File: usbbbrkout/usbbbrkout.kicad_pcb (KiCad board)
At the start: 4 copper layers, 27.7 x 20.3 mm, 12 parts, among them P101 CONN_01X01, P102 CONN_01X01, P103 CONN_01X01, P104 CONN_01X01, P105 USB_B

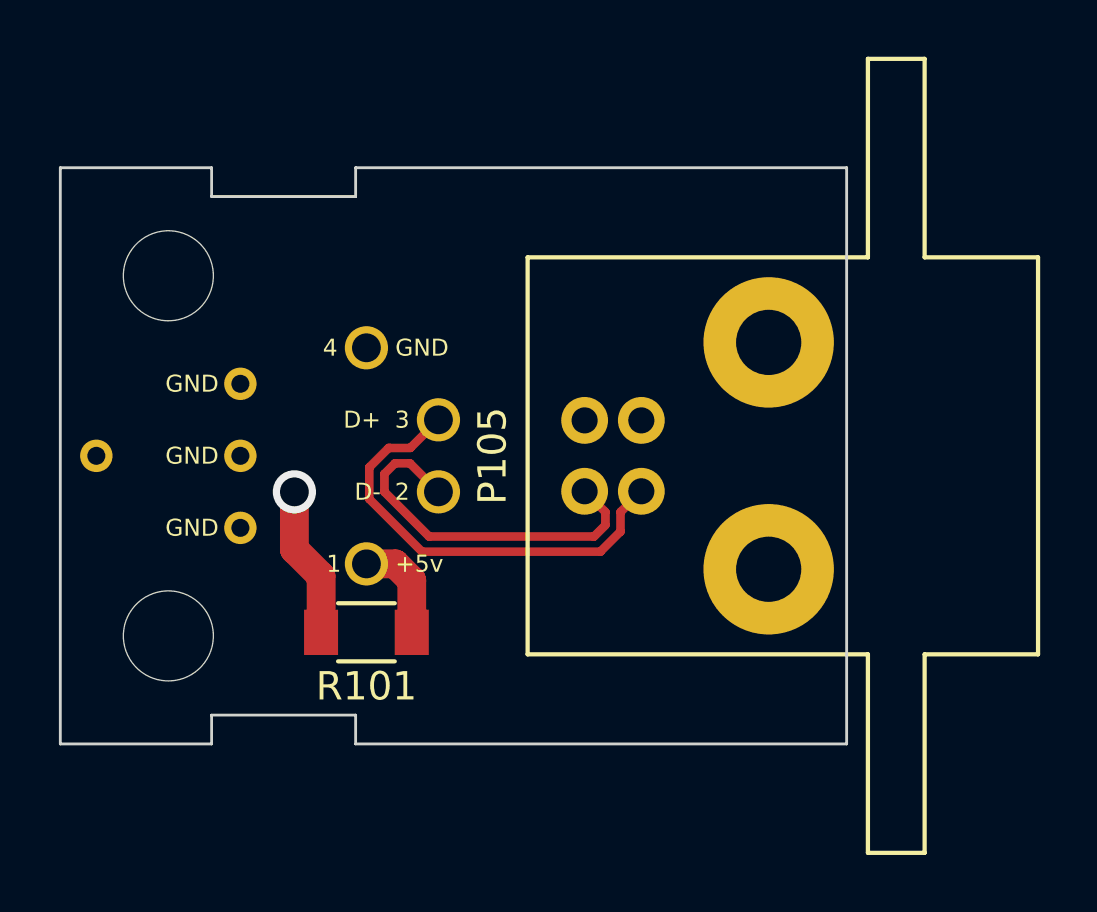
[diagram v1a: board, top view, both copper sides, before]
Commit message: Adjust clearances of ground and vcc pours.
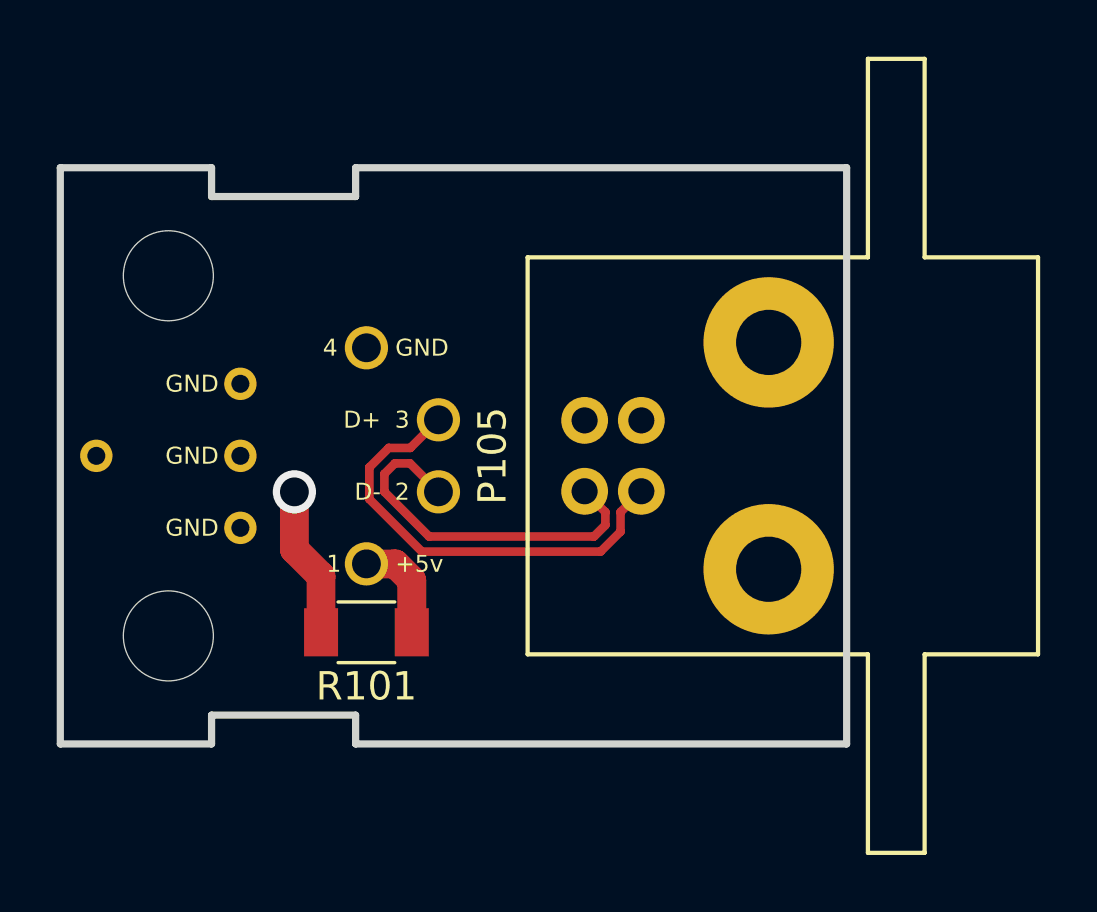
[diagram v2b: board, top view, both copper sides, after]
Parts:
- R101: footprint local:C_1206_HandSoldering -> local:R_1206_HandSoldering
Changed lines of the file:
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@@
   )
   (setup
-    (last_trace_width 0.254)
+    (last_trace_width 1.016)
     (user_trace_width 0.254)
     (user_trace_width 0.381)
@@
     )
     (fp_circle (center 0 0) (end 3.81 0) (layer Cmts.User) (width 0.381))
-    (pad "" np_thru_hole circle (at 0 0) (size 3.175 3.175) (drill 3.175) (layers *.Cu *.Mask))
+    (pad "" np_thru_hole circle (at 0 0) (size 3.175 3.175) (drill 3.175) (layers *.Cu *.Mask)
+      (clearance 0.508))
   )
   (module local:MountingHole_125mil locked (layer F.Cu)
@@
     )
     (fp_circle (center 0 0) (end 3.81 0) (layer Cmts.User) (width 0.381))
-    (pad "" np_thru_hole circle (at 0 0) (size 3.175 3.175) (drill 3.175) (layers *.Cu *.Mask))
+    (pad "" np_thru_hole circle (at 0 0) (size 3.175 3.175) (drill 3.175) (layers *.Cu *.Mask)
+      (clearance 0.508))
   )
   (module local:Stitching_Via_40x24mil locked (layer F.Cu)
@@
     )
   )
-  (module local:C_1206_HandSoldering (layer F.Cu)
+  (module local:R_1206_HandSoldering (layer F.Cu)
     (at 139.065 107.823)
-    (descr "Capacitor SMD 1206, hand soldering")
-    (tags "capacitor 1206")
+    (descr "Resistor SMD 1206, hand soldering")
+    (tags "resistor 1206")
     (attr smd)
     (fp_text reference R101 (at 0 1.905) (layer F.SilkS)
       (effects (font (size 1 1) (thickness 0.15)))
     )
-    (fp_text value 0R (at 0 2.3) (layer F.Fab)
-      (effects (font (size 1 1) (thickness 0.15)))
-    )
-    (fp_line (start -2.5 -1.15) (end 2.5 -1.15) (layer F.CrtYd) (width 0.05))
-    (fp_line (start -2.5 1.15) (end 2.5 1.15) (layer F.CrtYd) (width 0.05))
-    (fp_line (start -2.5 -1.15) (end -2.5 1.15) (layer F.CrtYd) (width 0.05))
-    (fp_line (start 2.5 -1.15) (end 2.5 1.15) (layer F.CrtYd) (width 0.05))
-    (fp_line (start 1 -1.025) (end -1 -1.025) (layer F.SilkS) (width 0.15))
-    (fp_line (start -1 1.025) (end 1 1.025) (layer F.SilkS) (width 0.15))
-    (pad 1 smd rect (at -1.6 0) (size 1.2 1.6) (layers F.Cu F.Paste F.Mask)
+    (fp_text value 0R (at 0 1.9) (layer F.Fab)
+      (effects (font (size 1 1) (thickness 0.15)))
+    )
+    (fp_text user %R (at 0 0) (layer F.Fab)
+      (effects (font (size 0.7 0.7) (thickness 0.105)))
+    )
+    (fp_line (start -1.6 0.8) (end -1.6 -0.8) (layer F.Fab) (width 0.1))
+    (fp_line (start 1.6 0.8) (end -1.6 0.8) (layer F.Fab) (width 0.1))
+    (fp_line (start 1.6 -0.8) (end 1.6 0.8) (layer F.Fab) (width 0.1))
+    (fp_line (start -1.6 -0.8) (end 1.6 -0.8) (layer F.Fab) (width 0.1))
+    (fp_line (start 1 1.07) (end -1 1.07) (layer F.SilkS) (width 0.12))
+    (fp_line (start -1 -1.07) (end 1 -1.07) (layer F.SilkS) (width 0.12))
+    (fp_line (start -3.25 -1.11) (end 3.25 -1.11) (layer F.CrtYd) (width 0.05))
+    (fp_line (start -3.25 -1.11) (end -3.25 1.1) (layer F.CrtYd) (width 0.05))
+    (fp_line (start 3.25 1.1) (end 3.25 -1.11) (layer F.CrtYd) (width 0.05))
+    (fp_line (start 3.25 1.1) (end -3.25 1.1) (layer F.CrtYd) (width 0.05))
+    (pad 1 smd rect (at -1.6 0) (size 1.2 1.7) (layers F.Cu F.Paste F.Mask)
       (net 4 VCC))
-    (pad 2 smd rect (at 1.6 0) (size 1.2 1.6) (layers F.Cu F.Paste F.Mask)
+    (pad 2 smd rect (at 1.6 0) (size 1.2 1.7) (layers F.Cu F.Paste F.Mask)
       (net 5 /+5v))
-    (model Capacitors_SMD.3dshapes/C_1206_HandSoldering.wrl
+    (model ${KISYS3DMOD}/Resistors_SMD.3dshapes/R_1206.wrl
       (at (xyz 0 0 0))
       (scale (xyz 1 1 1))
@@
     (effects (font (size 0.6 0.6) (thickness 0.127)) (justify right))
   )
-  (gr_line (start 133.604 111.76) (end 128.27 111.76) (layer Edge.Cuts) (width 0.1))
-  (gr_line (start 133.604 91.44) (end 128.27 91.44) (layer Edge.Cuts) (width 0.1))
-  (gr_line (start 138.684 110.744) (end 138.684 111.76) (layer Edge.Cuts) (width 0.1))
-  (gr_line (start 133.604 110.744) (end 138.684 110.744) (layer Edge.Cuts) (width 0.1))
-  (gr_line (start 133.604 111.76) (end 133.604 110.744) (layer Edge.Cuts) (width 0.1))
-  (gr_line (start 138.684 92.456) (end 138.684 91.44) (layer Edge.Cuts) (width 0.1))
-  (gr_line (start 133.604 92.456) (end 138.684 92.456) (layer Edge.Cuts) (width 0.1))
-  (gr_line (start 133.604 91.44) (end 133.604 92.456) (layer Edge.Cuts) (width 0.1))
+  (gr_line (start 133.604 111.76) (end 128.27 111.76) (layer Edge.Cuts) (width 0.254))
+  (gr_line (start 133.604 91.44) (end 128.27 91.44) (layer Edge.Cuts) (width 0.254))
+  (gr_line (start 138.684 110.744) (end 138.684 111.76) (layer Edge.Cuts) (width 0.254))
+  (gr_line (start 133.604 110.744) (end 138.684 110.744) (layer Edge.Cuts) (width 0.254))
+  (gr_line (start 133.604 111.76) (end 133.604 110.744) (layer Edge.Cuts) (width 0.254))
+  (gr_line (start 138.684 92.456) (end 138.684 91.44) (layer Edge.Cuts) (width 0.254))
+  (gr_line (start 133.604 92.456) (end 138.684 92.456) (layer Edge.Cuts) (width 0.254))
+  (gr_line (start 133.604 91.44) (end 133.604 92.456) (layer Edge.Cuts) (width 0.254))
   (gr_text "USB-B Breakout" (at 142.748 93.726) (layer B.SilkS)
     (effects (font (size 1 1) (thickness 0.15)) (justify mirror))
@@
     (effects (font (size 0.8 0.8) (thickness 0.15)) (justify mirror))
   )
-  (gr_line (start 156 91.44) (end 156 111.76) (layer Edge.Cuts) (width 0.1))
-  (gr_line (start 138.684 91.44) (end 156 91.44) (layer Edge.Cuts) (width 0.1))
-  (gr_line (start 128.27 111.76) (end 128.27 91.44) (layer Edge.Cuts) (width 0.1))
-  (gr_line (start 156 111.76) (end 138.684 111.76) (layer Edge.Cuts) (width 0.1))
+  (gr_line (start 156 91.44) (end 156 111.76) (layer Edge.Cuts) (width 0.254))
+  (gr_line (start 138.684 91.44) (end 156 91.44) (layer Edge.Cuts) (width 0.254))
+  (gr_line (start 128.27 111.76) (end 128.27 91.44) (layer Edge.Cuts) (width 0.254))
+  (gr_line (start 156 111.76) (end 138.684 111.76) (layer Edge.Cuts) (width 0.254))
   (segment (start 146.76 102.85) (end 147.493301 103.583301) (width 0.3048) (layer F.Cu) (net 2))
   (segment (start 147.493301 103.583301) (end 147.493301 104.042899) (width 0.3048) (layer F.Cu) (net 2))
@@
   (segment (start 139.8524 101.3206) (end 140.6144 101.3206) (width 0.3048) (layer F.Cu) (net 3))
   (segment (start 140.6144 101.3206) (end 141.605 100.33) (width 0.3048) (layer F.Cu) (net 3))
+  (segment (start 137.465 105.842) (end 137.465 107.823) (width 1.016) (layer F.Cu) (net 4))
   (via (at 136.525 102.87) (size 1.524) (drill 1.016) (layers F.Cu B.Cu) (net 4))
-  (segment (start 137.465 105.842) (end 137.465 107.823) (width 1.016) (layer F.Cu) (net 4))
   (segment (start 136.525 102.87) (end 136.525 104.902) (width 1.016) (layer F.Cu) (net 4))
   (segment (start 136.525 104.902) (end 137.465 105.842) (width 1.016) (layer F.Cu) (net 4))
+  (segment (start 140.665 105.994) (end 140.665 107.823) (width 1.016) (layer F.Cu) (net 5))
   (segment (start 139.065 105.41) (end 140.081 105.41) (width 1.016) (layer F.Cu) (net 5))
   (segment (start 140.081 105.41) (end 140.665 105.994) (width 1.016) (layer F.Cu) (net 5))
-  (segment (start 140.665 105.994) (end 140.665 107.823) (width 1.016) (layer F.Cu) (net 5))
   (zone (net 1) (net_name GND) (layer In1.Cu) (hatch edge 0.508)
     (connect_pads (clearance 0.253746))

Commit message: Update usbbbrkout design to KiCad 8.
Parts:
- P101, P102, P103, P104: footprint local:wire_60x40mil -> Local:wire_60x40mil
- P105: footprint local:usb-b-pm -> Local:usb-b-pm
- R101: footprint local:R_1206_HandSoldering -> Local:R_1206_HandSoldering
- REF** (x2): footprint local:MountingHole_125mil -> Local:MountingHole_125mil
- REF** (x4): footprint local:Stitching_Via_40x24mil -> Local:Stitching_Via_40x24mil
- turned P105 to 0 degrees
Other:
- net class Default removed
- net class Diff Pair removed
- net class minimum removed
- board text added: "dsun7c4osh@gmail.com"
- board text removed: "dcsun88osh@gmail.com"

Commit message: Bump version string of usbbbrkout to v1.1.0.
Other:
- board text added: "v1.1.0"
- board text removed: "v1.0.0"
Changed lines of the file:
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@@
 	(title_block
 		(title "USB-B panel mount breakout")
-		(date "2018-04-24")
-		(rev "v1.0.0")
+		(date "2025-01-27")
+		(rev "v1.1.0")
 	)
 	(layers
@@
 		(property ki_fp_filters "Connector*:*_1x??_*")
 		(sheetname "Root")
-		(sheetfile "/home/guest/cae/kicad/usbbbrkout/usbbbrkout.sch")
+		(sheetfile "usbbbrkout.kicad_sch")
 		(attr through_hole)
 		(pad "1" thru_hole circle
@@
 		(property ki_fp_filters "Connector*:*_1x??_*")
 		(sheetname "Root")
-		(sheetfile "/home/guest/cae/kicad/usbbbrkout/usbbbrkout.sch")
+		(sheetfile "usbbbrkout.kicad_sch")
 		(attr through_hole)
 		(pad "1" thru_hole circle
@@
 		(property ki_fp_filters "Connector*:*_1x??_*")
 		(sheetname "Root")
-		(sheetfile "/home/guest/cae/kicad/usbbbrkout/usbbbrkout.sch")
+		(sheetfile "usbbbrkout.kicad_sch")
 		(attr through_hole)
 		(pad "1" thru_hole circle
@@
 		(property ki_fp_filters "Connector*:*_1x??_*")
 		(sheetname "Root")
-		(sheetfile "/home/guest/cae/kicad/usbbbrkout/usbbbrkout.sch")
+		(sheetfile "usbbbrkout.kicad_sch")
 		(attr through_hole)
 		(pad "1" thru_hole circle
@@
 			)
 		)
+		(property "Voltage" ""
+			(at 0 0 0)
+			(unlocked yes)
+			(layer "F.Fab")
+			(hide yes)
+			(effects
+				(font
+					(size 1 1)
+					(thickness 0.15)
+				)
+			)
+		)
+		(property "Tolerance" ""
+			(at 0 0 0)
+			(unlocked yes)
+			(layer "F.Fab")
+			(hide yes)
+			(effects
+				(font
+					(size 1 1)
+					(thickness 0.15)
+				)
+			)
+		)
+		(property "Dielectric" ""
+			(at 0 0 0)
+			(unlocked yes)
+			(layer "F.Fab")
+			(hide yes)
+			(effects
+				(font
+					(size 1 1)
+					(thickness 0.15)
+				)
+			)
+		)
+		(property "Power" ""
+			(at 0 0 0)
+			(unlocked yes)
+			(layer "F.Fab")
+			(hide yes)
+			(effects
+				(font
+					(size 1 1)
+					(thickness 0.15)
+				)
+			)
+		)
+		(property "Current" ""
+			(at 0 0 0)
+			(unlocked yes)
+			(layer "F.Fab")
+			(hide yes)
+			(effects
+				(font
+					(size 1 1)
+					(thickness 0.15)
+				)
+			)
+		)
+		(property "Frequency" ""
+			(at 0 0 0)
+			(unlocked yes)
+			(layer "F.Fab")
+			(hide yes)
+			(effects
+				(font
+					(size 1 1)
+					(thickness 0.15)
+				)
+			)
+		)
 		(property ki_fp_filters "USB*")
 		(sheetname "Root")
-		(sheetfile "/home/guest/cae/kicad/usbbbrkout/usbbbrkout.sch")
+		(sheetfile "usbbbrkout.kicad_sch")
 		(attr through_hole)
 		(fp_line
@@
 		(property ki_fp_filters "R_* Resistor_*")
 		(sheetname "Root")
-		(sheetfile "/home/guest/cae/kicad/usbbbrkout/usbbbrkout.sch")
+		(sheetfile "usbbbrkout.kicad_sch")
 		(attr smd)
 		(fp_line
@@
 		(layer "Edge.Cuts")
 	)
-	(gr_text "v1.0.0"
+	(gr_text "v1.1.0"
 		(at 142.494 94.996 0)
 		(layer "B.SilkS")
